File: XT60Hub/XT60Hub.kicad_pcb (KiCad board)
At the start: 2 copper layers, 84.8 x 32.1 mm, 26 parts, among them J1 IN, J2 OUT1, J3 OUT2, J4 OUT3, J5 OUT4, J6 OUT5

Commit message: [XT60Hub] : 発注前に最終調整
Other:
- board text added: "ver 1.0: 2025-04-12"
- board text removed: "ver 1.0: 2025-04-07"

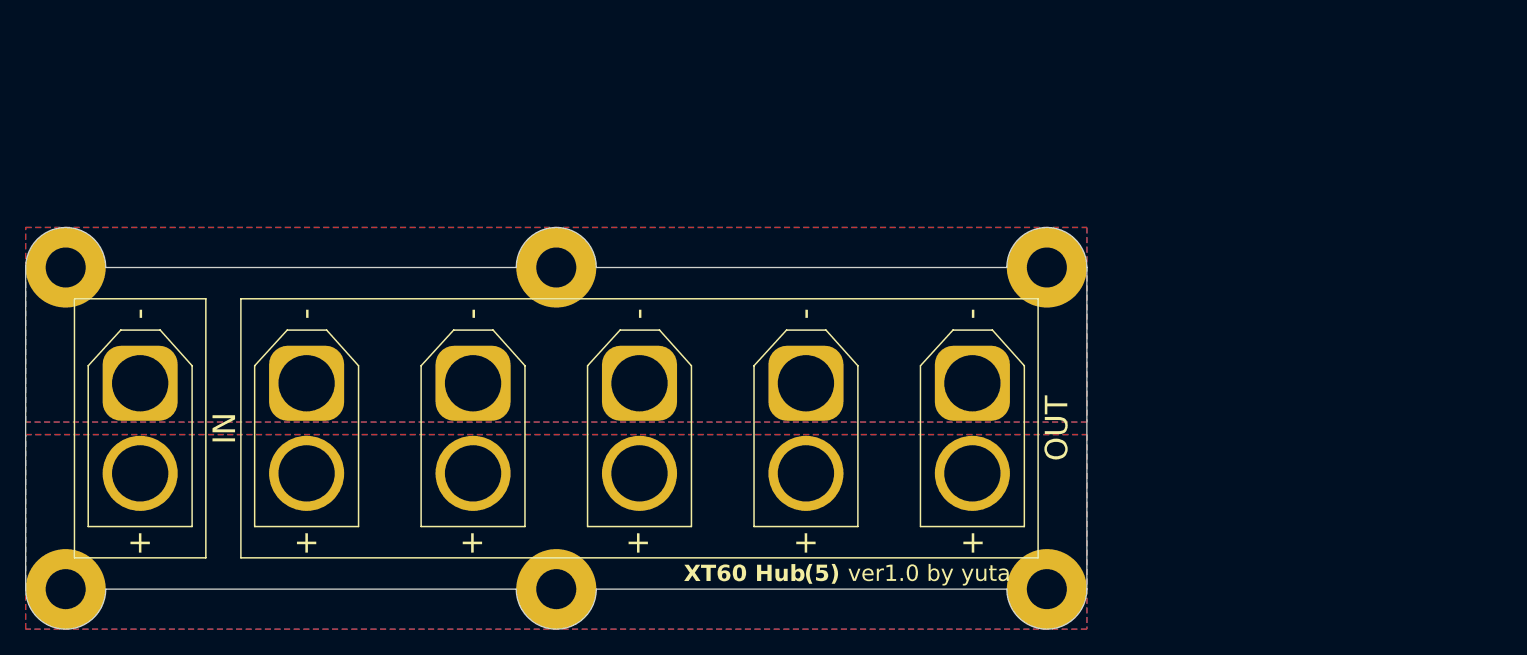
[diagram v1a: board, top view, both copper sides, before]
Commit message: XT60 Hub ver1.1
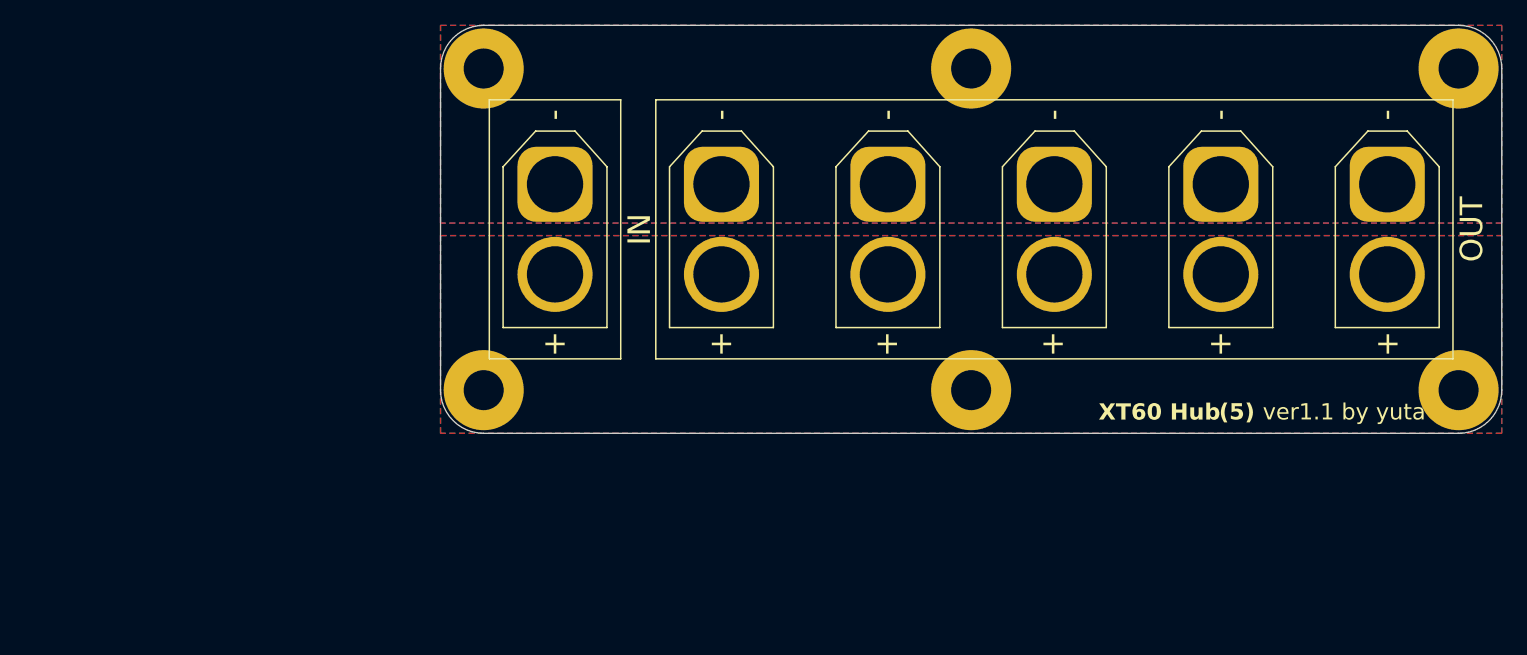
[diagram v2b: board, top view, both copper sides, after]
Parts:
- moved REF** 38.2 mm to (166.7, 86.1)
- moved H1 37.0 mm to (107.4, 85.9)
- moved H4 37.0 mm to (107.4, 111.6)
- moved J2 36.8 mm to (126.4, 95.2)
- moved J4 36.8 mm to (153.0, 95.2)
- moved J5 36.8 mm to (166.3, 95.2)
- moved J6 36.8 mm to (179.6, 95.2)
- moved H5 36.8 mm to (146.3, 111.6)
- moved H2 36.8 mm to (146.3, 85.9)
- moved J1 36.8 mm to (113.1, 95.2)
- moved J3 36.8 mm to (139.7, 95.2)
- moved H6 36.5 mm to (185.3, 111.6)
- moved H3 36.5 mm to (185.3, 85.9)
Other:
- board size 84.8 x 32.1 mm -> 84.8 x 32.6 mm
- board text added: "ver 1.1: 2025-09-10"
- board text added: "ver1.1 by yuta"
- board text removed: "ver 1.0: 2025-04-12"
- board text removed: "ver1.0 by yuta"
